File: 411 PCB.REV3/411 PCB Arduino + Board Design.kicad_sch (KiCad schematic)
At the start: 27 parts, among them J1 ICSP CONN, J3 Conn_01x04, J4 HEADER-1X770MIL, Q1 Q_NMOS_GDS, SW1 SW_SPST, SW2 SW_MEC_5E, U2 ATmega328P-P, Y1 8 MHz

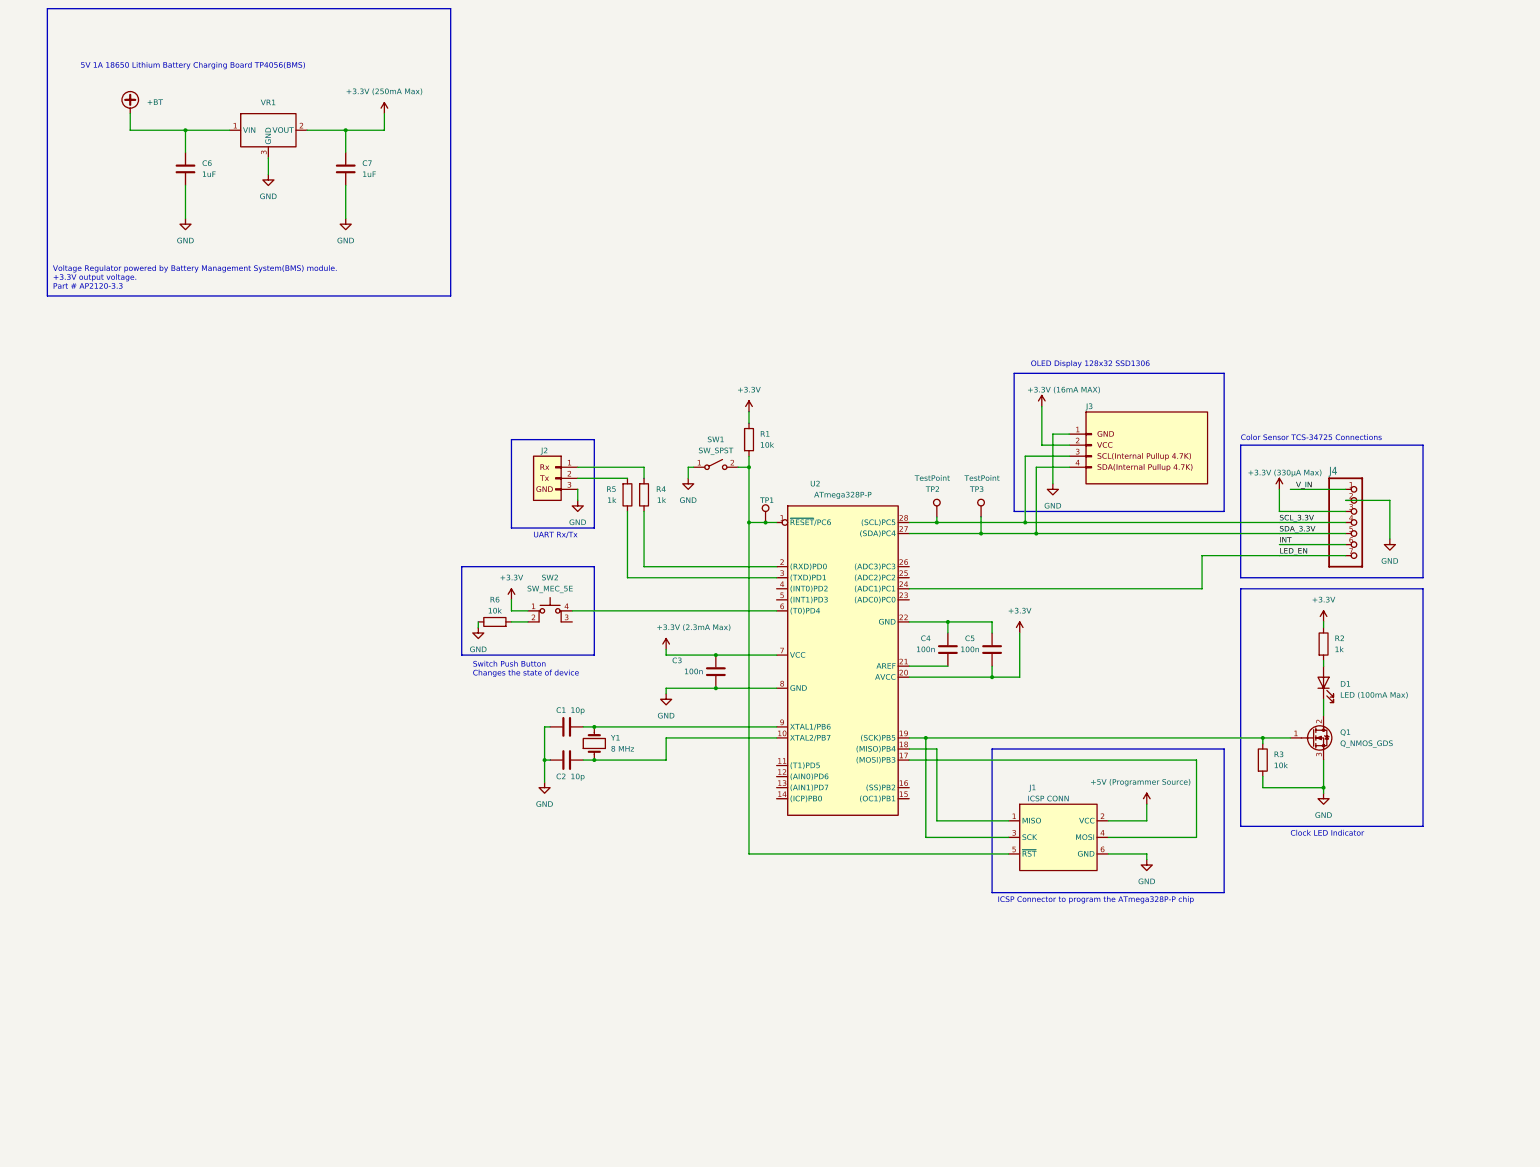
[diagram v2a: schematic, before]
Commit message: Fixed debounce error and added more test points to schematic
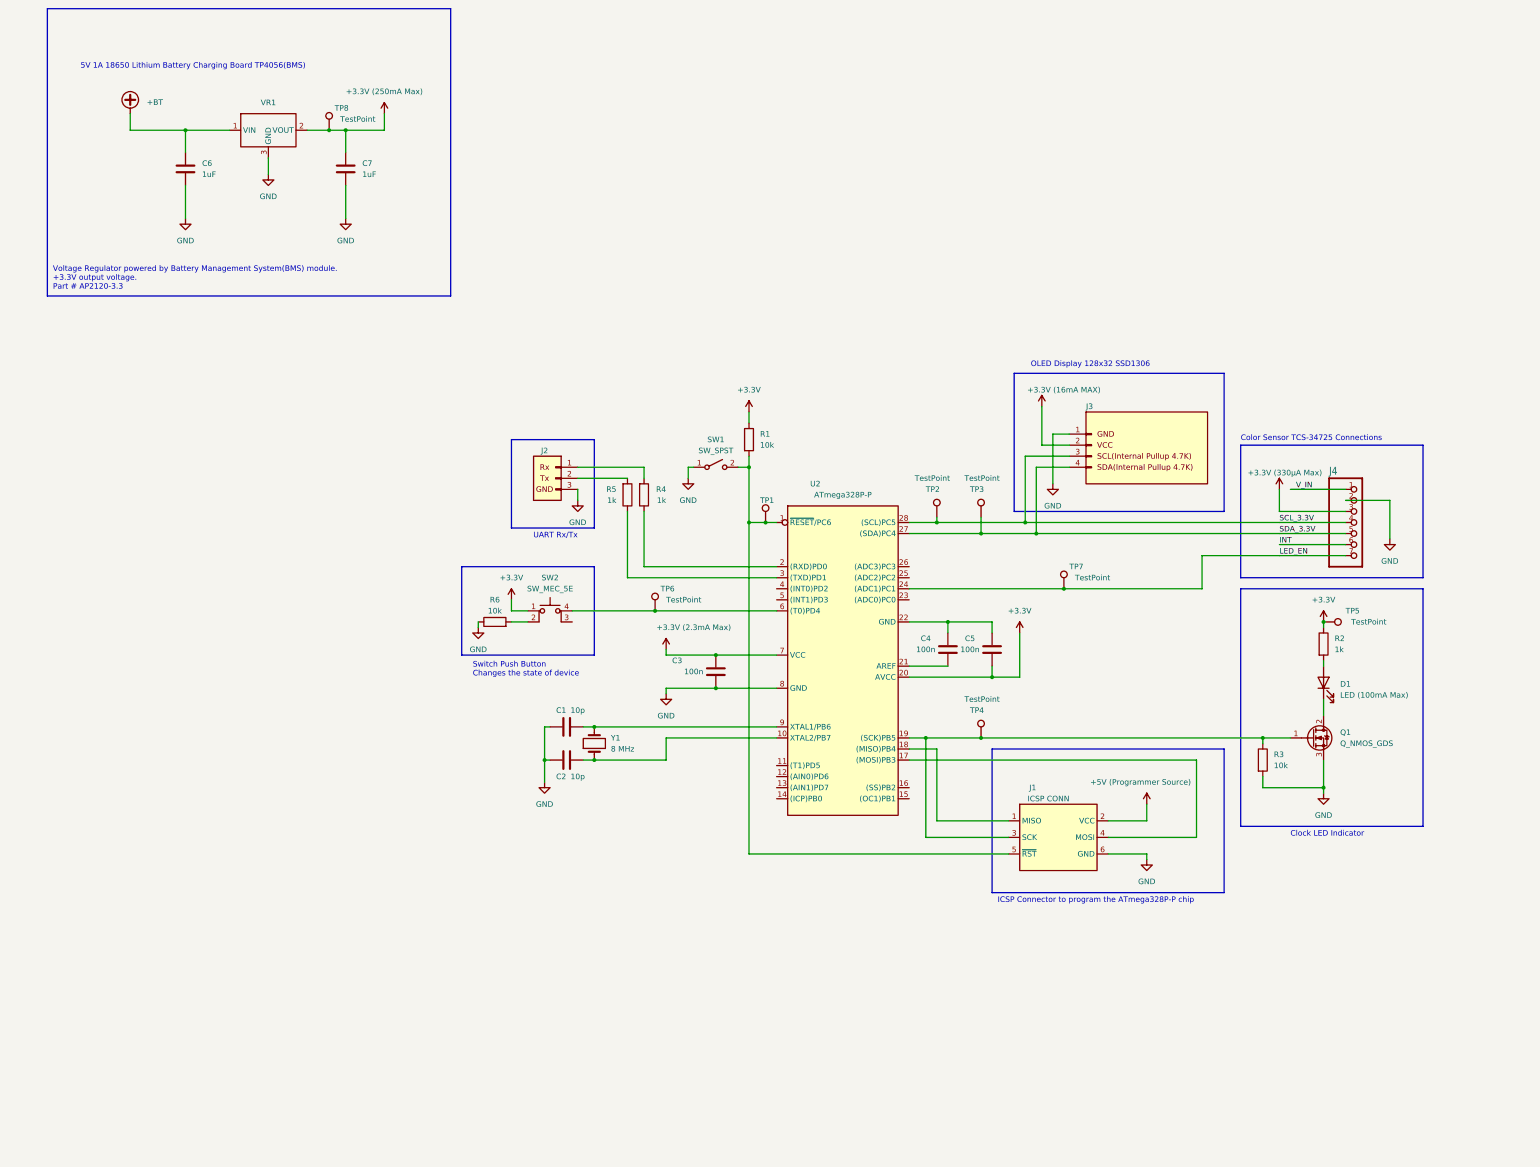
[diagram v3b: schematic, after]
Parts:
- added TP4, TP5, TP6, TP7, TP8: TestPoint, Connector_PinHeader_1.00mm:PinHeader_1x01_P1.00mm_Vertical, symbol Connector:TestPoint
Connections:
- net +3.3V: now also TP5.1, TP8.1
- net LED_EN: now also TP7.1
- net at SW2.4 (A), U2.6 ((T0)PD4): now also TP6.1
- net at J1.3 (SCK), Q1.1 (G), R3.1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: now also TP4.1
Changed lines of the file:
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@@
   (junction (at 132.08 99.06) (diameter 0) (color 0 0 0 0)
   )
+  (junction (at 393.7 212.09) (diameter 0) (color 0 0 0 0)
+  )
   (junction (at 261.62 176.53) (diameter 0) (color 0 0 0 0)
   )
+  (junction (at 165.1 99.06) (diameter 0) (color 0 0 0 0)
+  )
   (junction (at 261.62 189.23) (diameter 0) (color 0 0 0 0)
   )
+  (junction (at 334.01 204.47) (diameter 0) (color 0 0 0 0)
+  )
   (junction (at 379.73 238.76) (diameter 0) (color 0 0 0 0)
   )
   (junction (at 317.5 224.79) (diameter 0) (color 0 0 0 0)
   )
+  (junction (at 240.03 209.55) (diameter 0) (color 0 0 0 0)
+  )
   (junction (at 226.06 243.84) (diameter 0) (color 0 0 0 0)
   )
@@
   )
   (junction (at 325.12 189.23) (diameter 0) (color 0 0 0 0)
+  )
+  (junction (at 314.96 238.76) (diameter 0) (color 0 0 0 0)
   )
   (junction (at 168.91 99.06) (diameter 0) (color 0 0 0 0)
@@
     (stroke (width 0) (type default))
   )
-  (wire (pts (xy 302.26 238.76) (xy 379.73 238.76))
+  (wire (pts (xy 302.26 238.76) (xy 314.96 238.76))
     (stroke (width 0) (type default))
   )
@@
     (stroke (width 0) (type default))
   )
-  (wire (pts (xy 298.45 204.47) (xy 365.76 204.47))
+  (wire (pts (xy 298.45 204.47) (xy 334.01 204.47))
     (stroke (width 0) (type default))
   )
   (wire (pts (xy 317.5 224.79) (xy 317.5 222.25))
+    (stroke (width 0) (type default))
+  )
+  (wire (pts (xy 165.1 99.06) (xy 168.91 99.06))
     (stroke (width 0) (type default))
   )
@@
     (stroke (width 0) (type default))
   )
+  (wire (pts (xy 240.03 209.55) (xy 267.97 209.55))
+    (stroke (width 0) (type default))
+  )
   (wire (pts (xy 398.78 184.15) (xy 408.94 184.15))
     (stroke (width 0.1524) (type solid))
@@
     (stroke (width 0) (type default))
   )
-  (wire (pts (xy 160.02 99.06) (xy 168.91 99.06))
+  (wire (pts (xy 160.02 99.06) (xy 165.1 99.06))
     (stroke (width 0) (type default))
   )
   (wire (pts (xy 248.92 176.53) (xy 247.65 176.53))
+    (stroke (width 0) (type default))
+  )
+  (wire (pts (xy 334.01 204.47) (xy 365.76 204.47))
     (stroke (width 0) (type default))
   )
@@
     (stroke (width 0) (type default))
   )
-  (wire (pts (xy 220.98 209.55) (xy 267.97 209.55))
+  (wire (pts (xy 220.98 209.55) (xy 240.03 209.55))
     (stroke (width 0) (type default))
   )
@@
   )
   (wire (pts (xy 393.7 220.98) (xy 393.7 222.25))
+    (stroke (width 0) (type default))
+  )
+  (wire (pts (xy 314.96 238.76) (xy 379.73 238.76))
     (stroke (width 0) (type default))
   )
@@
     )
   )
+  (symbol (lib_id "Connector:TestPoint") (at 334.01 204.47 0) (unit 1)
+    (in_bom yes) (on_board yes) (dnp no)
+    (property "Reference" "TP7" (at 335.28 199.39 0)
+      (effects (font (size 1.27 1.27)) (justify left))
+    )
+    (property "Value" "TestPoint" (at 336.55 201.93 0)
+      (effects (font (size 1.27 1.27)) (justify left))
+    )
+    (property "Footprint" "Connector_PinHeader_1.00mm:PinHeader_1x01_P1.00mm_Vertical" (at 339.09 204.47 0)
+      (effects (font (size 1.27 1.27)) hide)
+    )
+    (property "Datasheet" "~" (at 339.09 204.47 0)
+      (effects (font (size 1.27 1.27)) hide)
+    )
+    (pin "1")
+    (instances
+      (project "411 PCB Arduino + Board Design"
+        (path "/3b213592-ad28-4b80-bc7a-214b9fe026d8"
+          (reference "TP7") (unit 1)
+        )
+      )
+    )
+  )
   (symbol (lib_id "power:GND") (at 331.47 180.34 0) (unit 1)
     (in_bom yes) (on_board yes) (dnp no) (fields_autoplaced)
@@
     )
   )
+  (symbol (lib_id "Connector:TestPoint") (at 165.1 99.06 0) (unit 1)
+    (in_bom yes) (on_board yes) (dnp no)
+    (property "Reference" "TP8" (at 166.37 93.98 0)
+      (effects (font (size 1.27 1.27)) (justify left))
+    )
+    (property "Value" "TestPoint" (at 167.64 96.52 0)
+      (effects (font (size 1.27 1.27)) (justify left))
+    )
+    (property "Footprint" "Connector_PinHeader_1.00mm:PinHeader_1x01_P1.00mm_Vertical" (at 170.18 99.06 0)
+      (effects (font (size 1.27 1.27)) hide)
+    )
+    (property "Datasheet" "~" (at 170.18 99.06 0)
+      (effects (font (size 1.27 1.27)) hide)
+    )
+    (pin "1")
+    (instances
+      (project "411 PCB Arduino + Board Design"
+        (path "/3b213592-ad28-4b80-bc7a-214b9fe026d8"
+          (reference "TP8") (unit 1)
+        )
+      )
+    )
+  )
   (symbol (lib_id "power:GND") (at 408.94 193.04 0) (unit 1)
     (in_bom yes) (on_board yes) (dnp no) (fields_autoplaced)
@@
         (path "/3b213592-ad28-4b80-bc7a-214b9fe026d8"
           (reference "#PWR032") (unit 1)
+        )
+      )
+    )
+  )
+  (symbol (lib_id "Connector:TestPoint") (at 240.03 209.55 0) (unit 1)
+    (in_bom yes) (on_board yes) (dnp no)
+    (property "Reference" "TP6" (at 241.3 204.47 0)
+      (effects (font (size 1.27 1.27)) (justify left))
+    )
+    (property "Value" "TestPoint" (at 242.57 207.01 0)
+      (effects (font (size 1.27 1.27)) (justify left))
+    )
+    (property "Footprint" "Connector_PinHeader_1.00mm:PinHeader_1x01_P1.00mm_Vertical" (at 245.11 209.55 0)
+      (effects (font (size 1.27 1.27)) hide)
+    )
+    (property "Datasheet" "~" (at 245.11 209.55 0)
+      (effects (font (size 1.27 1.27)) hide)
+    )
+    (pin "1")
+    (instances
+      (project "411 PCB Arduino + Board Design"
+        (path "/3b213592-ad28-4b80-bc7a-214b9fe026d8"
+          (reference "TP6") (unit 1)
         )
       )
@@
     )
   )
+  (symbol (lib_id "Connector:TestPoint") (at 393.7 212.09 270) (unit 1)
+    (in_bom yes) (on_board yes) (dnp no)
+    (property "Reference" "TP5" (at 398.78 209.55 90)
+      (effects (font (size 1.27 1.27)) (justify left))
+    )
+    (property "Value" "TestPoint" (at 400.05 212.09 90)
+      (effects (font (size 1.27 1.27)) (justify left))
+    )
+    (property "Footprint" "Connector_PinHeader_1.00mm:PinHeader_1x01_P1.00mm_Vertical" (at 393.7 217.17 0)
+      (effects (font (size 1.27 1.27)) hide)
+    )
+    (property "Datasheet" "~" (at 393.7 217.17 0)
+      (effects (font (size 1.27 1.27)) hide)
+    )
+    (pin "1")
+    (instances
+      (project "411 PCB Arduino + Board Design"
+        (path "/3b213592-ad28-4b80-bc7a-214b9fe026d8"
+          (reference "TP5") (unit 1)
+        )
+      )
+    )
+  )
   (symbol (lib_id "power:GND") (at 353.06 266.7 0) (unit 1)
     (in_bom yes) (on_board yes) (dnp no)
@@
         )
       )
+    )
+  )
+  (symbol (lib_id "Connector:TestPoint") (at 314.96 238.76 0) (unit 1)
+    (in_bom yes) (on_board yes) (dnp no)
+    (property "Reference" "TP4" (at 312.42 232.41 0)
+      (effects (font (size 1.27 1.27)) (justify left))
+    )
+    (property "Value" "TestPoint" (at 311.15 229.87 0)
+      (effects (font (size 1.27 1.27)) (justify left))
+    )
+    (property "Footprint" "Connector_PinHeader_1.00mm:PinHeader_1x01_P1.00mm_Vertical" (at 320.04 238.76 0)
+      (effects (font (size 1.27 1.27)) hide)
+    )
+    (property "Datasheet" "~" (at 320.04 238.76 0)
+      (effects (font (size 1.27 1.27)) hide)
+    )
+    (pin "1")
+    (instances
+      (project "411 PCB Arduino + Board Design"
+        (path "/3b213592-ad28-4b80-bc7a-214b9fe026d8"
+          (reference "TP4") (unit 1)
+        )
+      )

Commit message: Rev4 Fixed Footprint and Schematic Layout a bit.
Monday 11/13/2023 Will do the PCB final routing
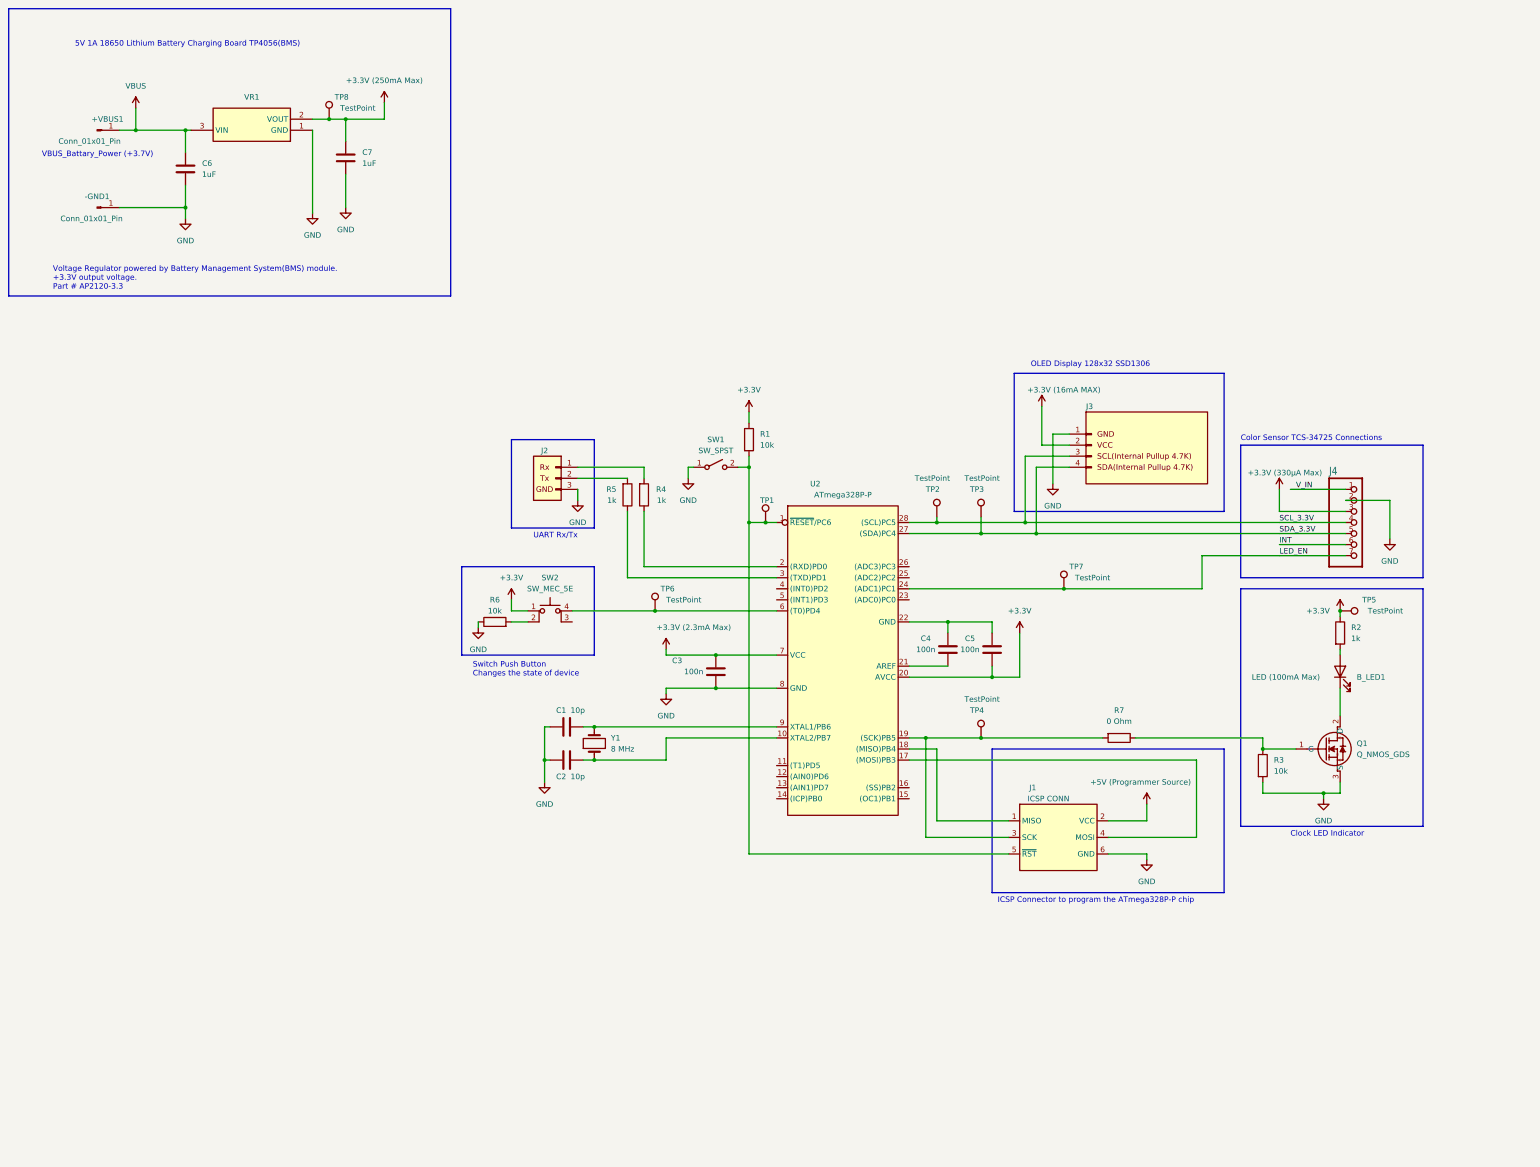
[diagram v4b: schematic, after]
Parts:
- added +VBUS1, -GND1: Conn_01x01_Pin, Connector_PinHeader_2.54mm:PinHeader_1x01_P2.54mm_Vertical, symbol Connector:Conn_01x01_Pin
- added R7: 0 Ohm, Resistor_THT:R_Axial_DIN0204_L3.6mm_D1.6mm_P5.08mm_Horizontal, symbol Device:R
- B_LED1: renamed from D1; footprint LED_SMD:LED_0805_2012Metric_Pad1.15x1.40mm_HandSolder -> LED_SMD:LTST-B680
- J1: footprint Connector_PinHeader_1.00mm:PinHeader_2x03_P1.00mm_Vertical -> PH2_06_UA:CONN_PH2-06-UA_ADM
- J2: footprint (none) -> Connector_PinHeader_2.54mm:PinHeader_1x03_P2.54mm_Vertical
- Q1: footprint Package_TO_SOT_SMD:SOT-323_SC-70_Handsoldering -> DMN63D9LW:SOIC_D8LW-13_DIO; symbol Device:Q_NMOS_GDS -> 2023-11-13_01-53-07:DMN63D8LW-13
- VR1: footprint Package_TO_SOT_SMD:SOT-23 -> SamacSys_Parts:SOT96P240X120-3N; symbol Regulator_Linear:AP2120-3.3 -> SamacSys_Parts:AP2120N-3.3TRG1; Arrow Part Number (none) -> AP2120N-3.3TRG1; Arrow Price/Stock (none) -> https://www.arrow.com/en/products/ap2120n-3.3trg1/diodes-in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; Height (none) -> 1.2; Manufacturer_Name (none) -> Diodes Inc.; Manufacturer_Part_Number (none) -> AP2120N-3.3TRG1; Mouser Part Number (none) -> 621-AP2120N-3.3TRG1; Mouser Price/Stock (none) -> https://www.mouser.co.uk/ProductDetail/Diodes-Incorporated/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
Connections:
- net GND: now also VR1.1 (GND), -GND1.1 (Pin_1); no longer VR1.3 (GND)
- net at J1.3 (SCK), TP4.1, U2.19 ((SCK)PB5): now also R7.2; no longer Q1.1 (G), R3.1
- net +VDC renamed VBUS
- net VBUS: now also VR1.3 (VIN), +VBUS1.1 (Pin_1); no longer VR1.1 (VIN)
- new net: Q1.1 (G), R3.1, R7.1
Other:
- note added: "VBUS_Battary_Power (+3.7V)"
- moved on the sheet: B_LED1, C7, R2, R3, TP5, TP8
